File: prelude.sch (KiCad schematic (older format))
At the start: 33 parts

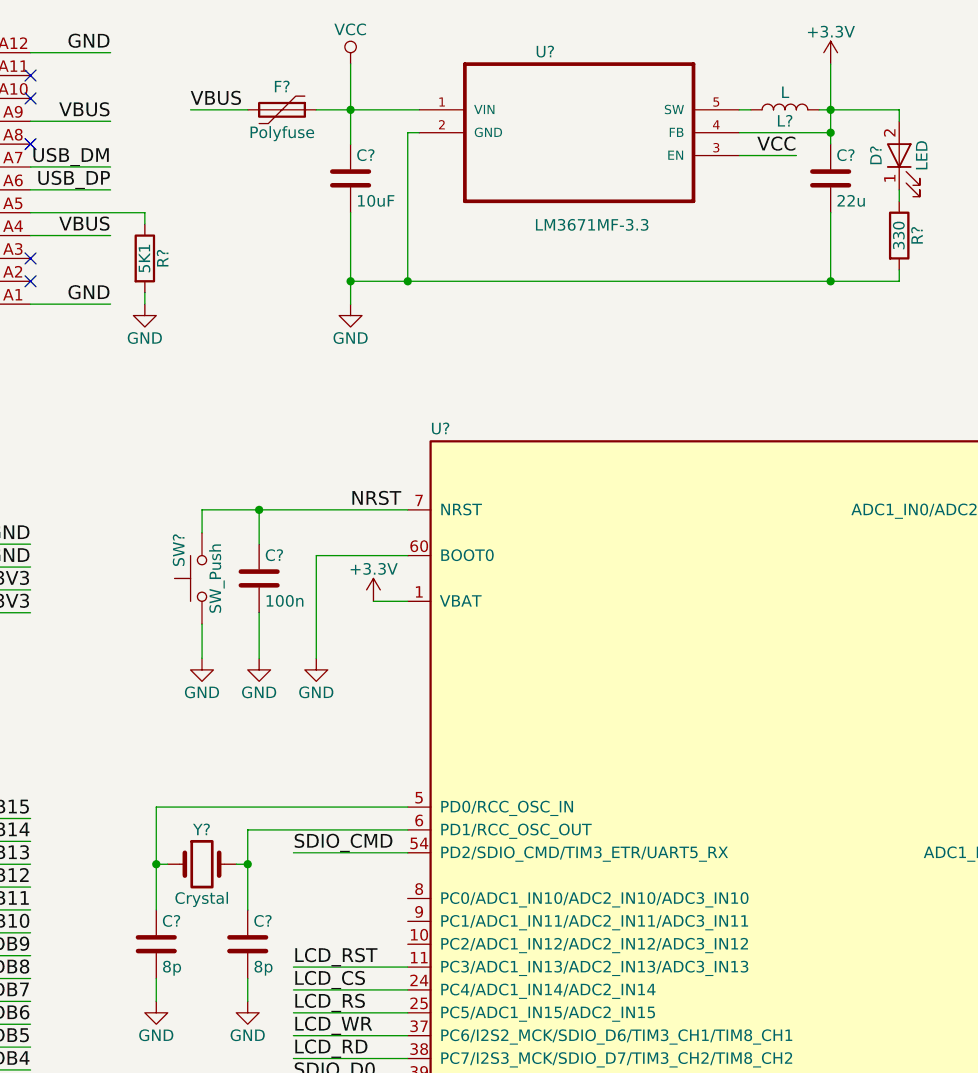
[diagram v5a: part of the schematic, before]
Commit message: Adds values to Crystal (16 MHz) and a one inductor (2.2 uH)
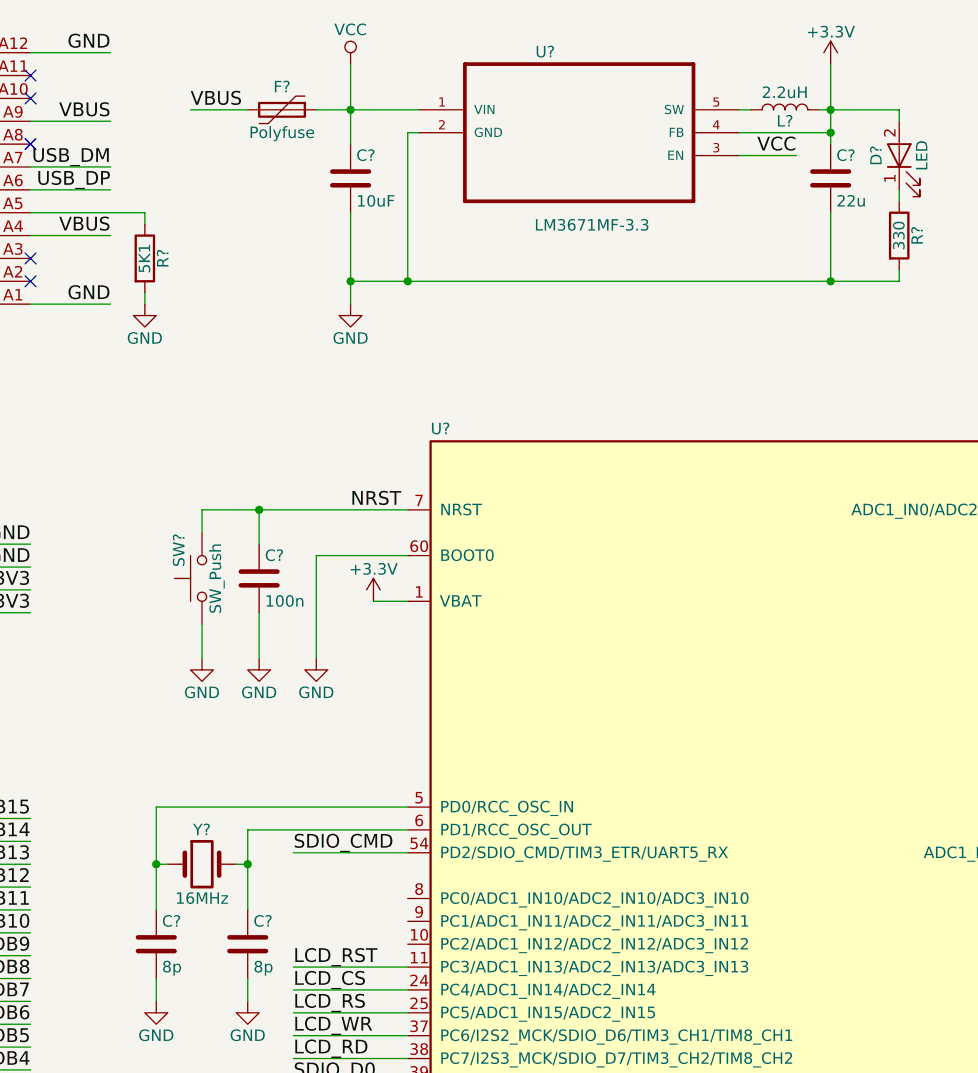
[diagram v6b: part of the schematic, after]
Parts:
- L?: value L -> 2.2uH
- Y?: value Crystal -> 16MHz
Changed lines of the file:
@@
 P 5600 1000
 F 0 "L?" V 5550 1000 50  0000 C CNN
-F 1 "L" V 5675 1000 50  0000 C CNN
+F 1 "2.2uH" V 5675 1000 50  0000 C CNN
 F 2 "" H 5600 1000 50  0001 C CNN
 F 3 "" H 5600 1000 50  0001 C CNN
@@
 P 3050 4300
 F 0 "Y?" H 3050 4450 50  0000 C CNN
-F 1 "Crystal" H 3050 4150 50  0000 C CNN
+F 1 "16MHz" H 3050 4150 50  0000 C CNN
 F 2 "" H 3050 4300 50  0001 C CNN
 F 3 "" H 3050 4300 50  0001 C CNN

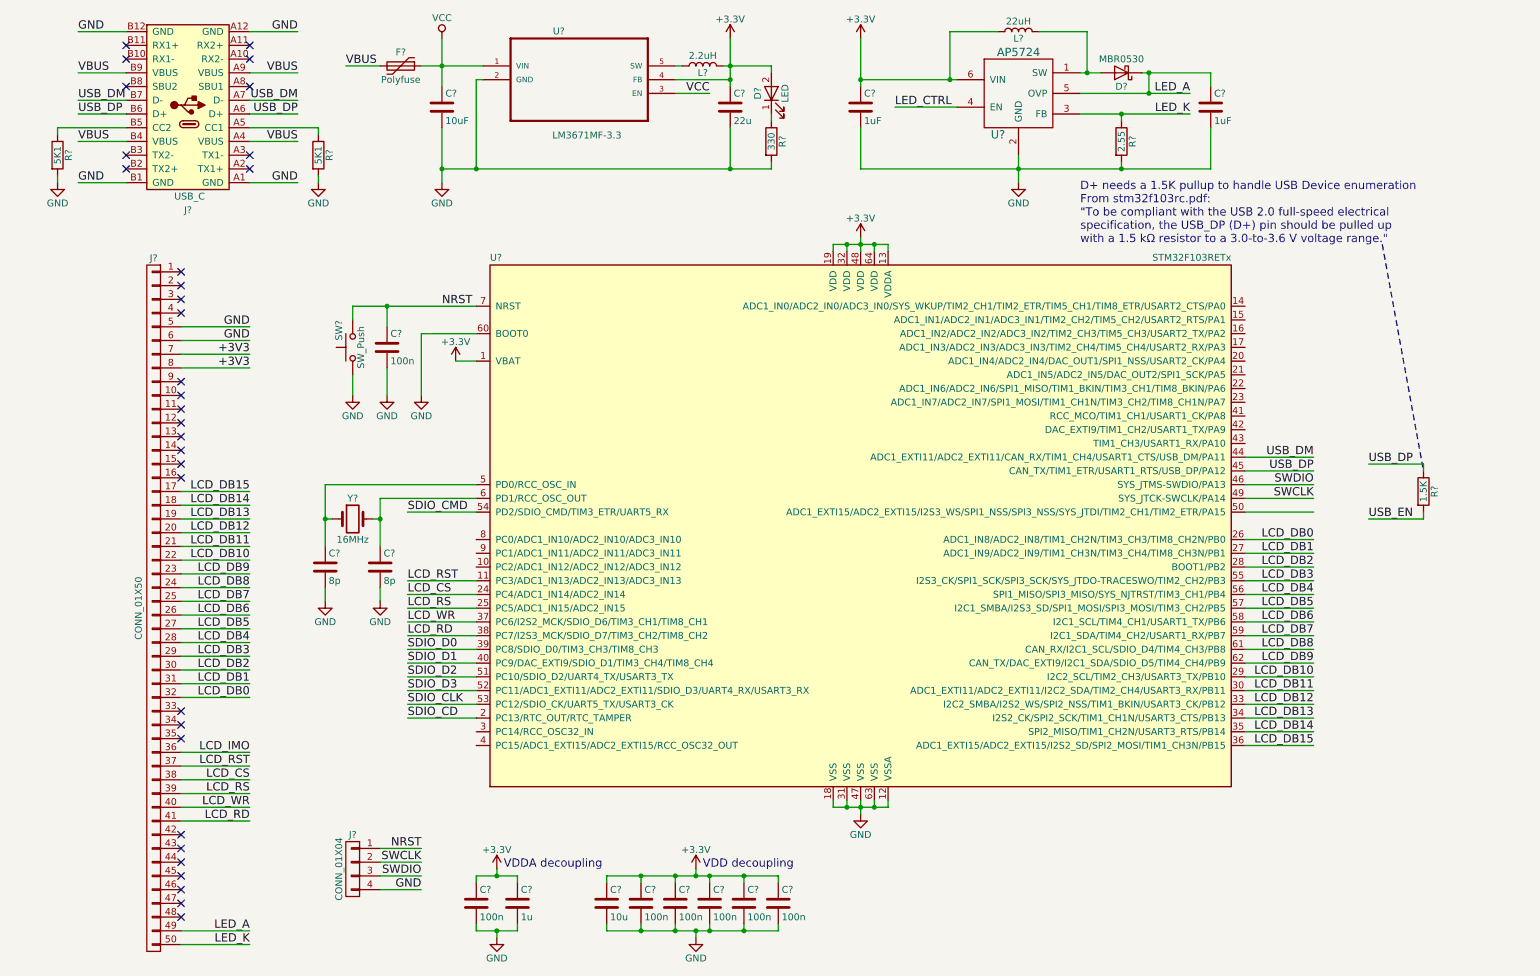
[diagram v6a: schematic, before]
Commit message: Annotates components
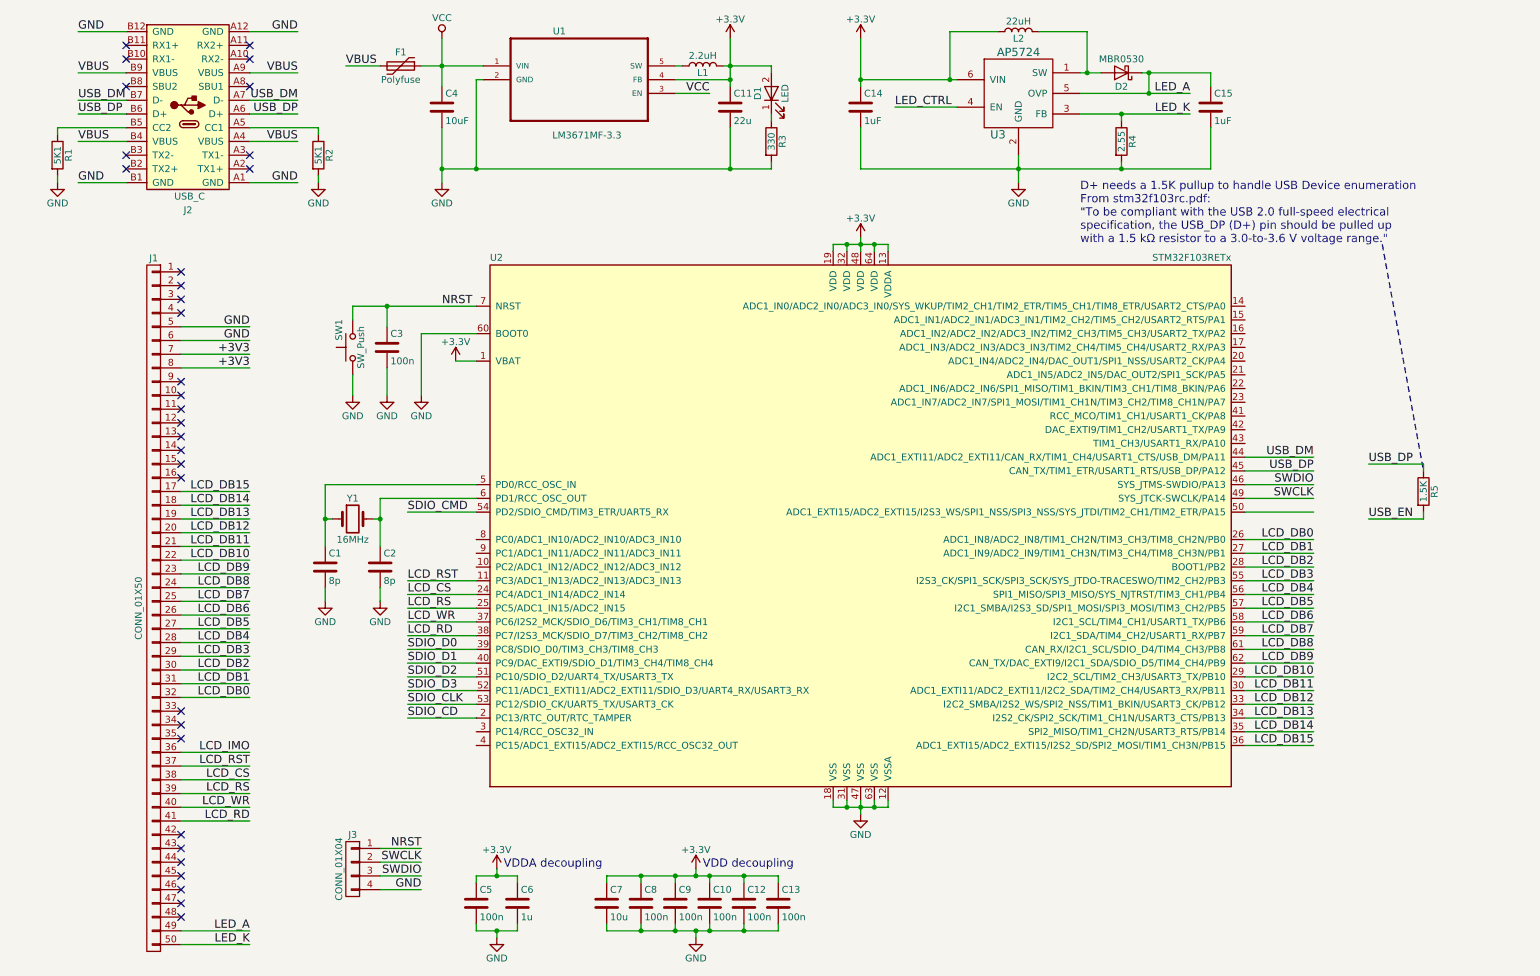
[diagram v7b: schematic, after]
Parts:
- gave numbers to parts that had none: 33

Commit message: Several changes
Ran CvPcb
Added MicroSD card connector (Molex)
Started PCB routing with MCU pin row pins 1-16 facing 50-pin LCD connector
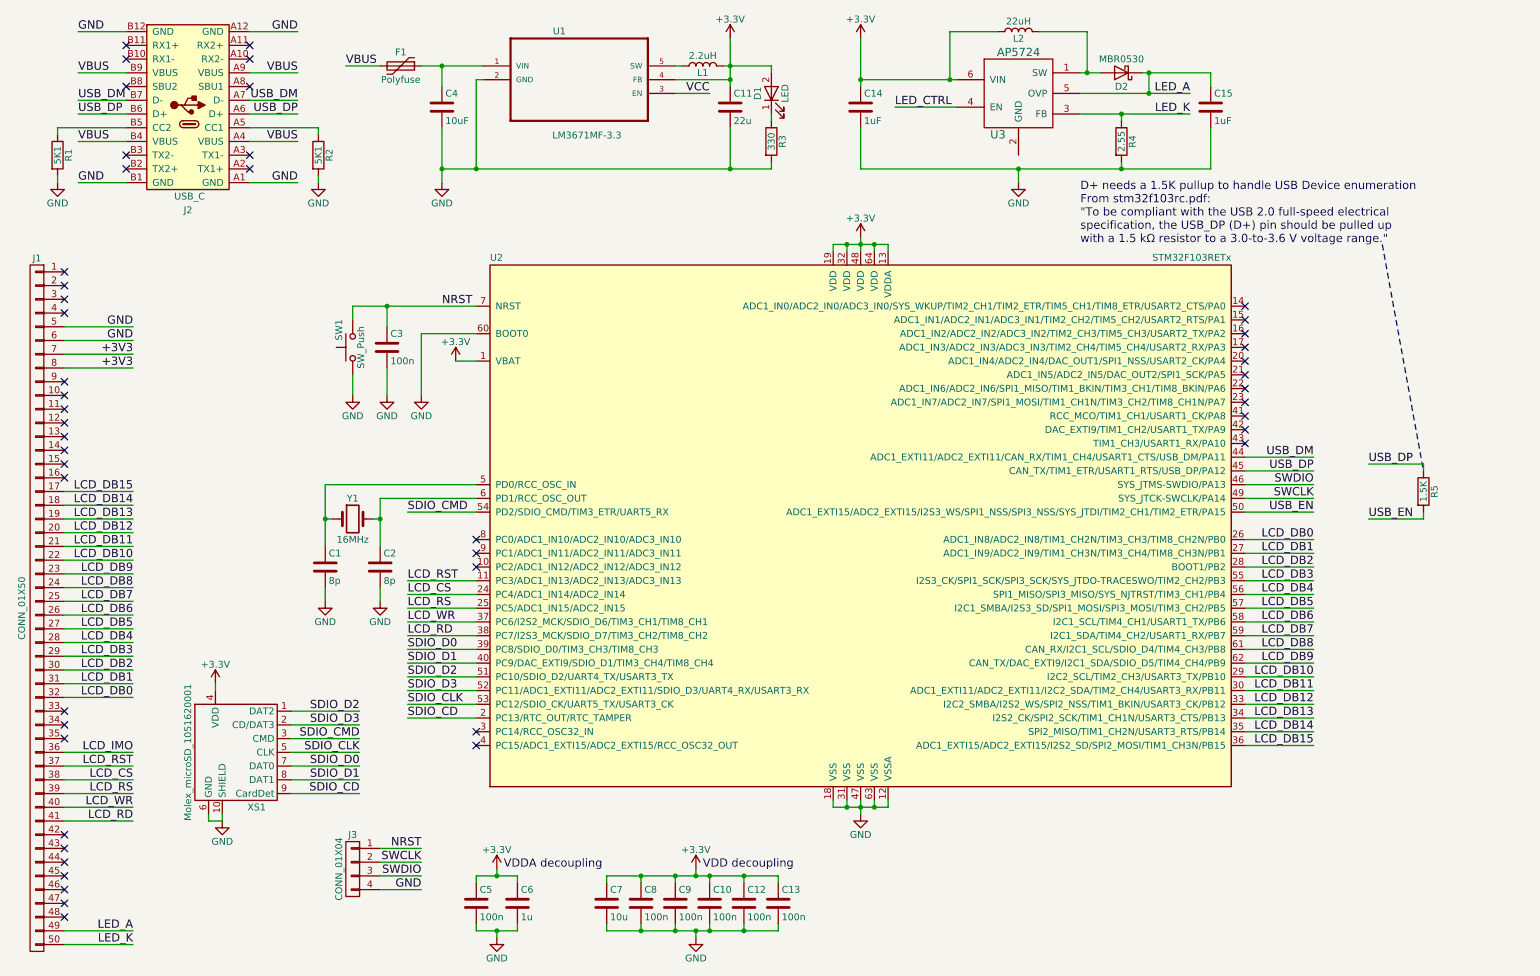
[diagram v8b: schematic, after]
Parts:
- added XS1: Molex_microSD_1051620001, volium:Molex_1051620001, symbol Molex_microSD_1051620001
- C1, C10, C11, C12, C13, C14, C15, C2, C3, C4, C5, C6, C7, C8, C9: footprint (none) -> Capacitors_SMD:C_0805
- D1: footprint (none) -> LEDs:LED_0805
- D2: footprint (none) -> Diodes_SMD:D_SOD-123
- F1: footprint (none) -> volium:MF-PSMF050X
- J1: footprint (none) -> volium:62684-502100ALF
- J2: footprint (none) -> volium:DX07S024XJ1
- J3: footprint (none) -> Pin_Headers:Pin_Header_Angled_1x04_Pitch2.54mm
- L1: footprint (none) -> Inductors:Inductor_Taiyo-Yuden_NR-24xx
- L2: footprint (none) -> Inductors:Inductor_Taiyo-Yuden_NR-30xx
- R1, R2, R3, R4, R5: footprint (none) -> Resistors_SMD:R_0805
- SW1: footprint (none) -> Buttons_Switches_SMD:SW_SPST_PTS645
- U1: footprint SOT95P284X122-5N -> TO_SOT_Packages_SMD:TSOT-23-5
- U2: footprint LQFP64 -> Housings_QFP:LQFP-64_10x10mm_Pitch0.5mm
- U3: footprint (none) -> TO_SOT_Packages_SMD:SOT-23-6
- Y1: footprint (none) -> Crystals:Crystal_SMD_5032-2pin_5.0x3.2mm
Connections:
- net +3V3: now also XS1.4 (VDD)
- net GND: now also XS1.10 (SHIELD), XS1.6 (GND); no longer U3.2 (GND)
- net SDIO_CD: now also XS1.9 (CardDet)
- net SDIO_CLK: now also XS1.5 (CLK)
- net SDIO_CMD: now also XS1.3 (CMD)
- net SDIO_D0: now also XS1.7 (DAT0)
- net SDIO_D1: now also XS1.8 (DAT1)
- net SDIO_D2: now also XS1.1 (DAT2)
- net SDIO_D3: now also XS1.2 (CD/DAT3)
- net USB_EN: now also U2.50 (ADC1_EXTI15/ADC2_EXTI15/I2S3_WS/SPI1_NSS/SPI3_NSS/SYS_JTDI/TIM2_CH1/TIM2_ETR/PA15)
- net VCC: no longer C4.1, F1.1, U1.1 (VIN)
- new net: C4.1, F1.1, U1.1 (VIN)
- no-connect marks 32 -> 48
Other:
- moved on the sheet: J1
